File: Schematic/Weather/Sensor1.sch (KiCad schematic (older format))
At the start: 2 parts

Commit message: Start PCB
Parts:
- MOD1: footprint (none) -> footprint:HTU21
- MOD2: footprint (none) -> footprint:BMP180
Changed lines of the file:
@@
 F 0 "MOD2" H 5678 1771 50  0000 L CNN
 F 1 "BMP180" H 5678 1680 50  0000 L CNN
-F 2 "" H 5250 1350 50  0001 C CNN
+F 2 "footprint:BMP180" H 5250 1350 50  0001 C CNN
 F 3 "" H 5250 1350 50  0001 C CNN
 	1    5050 1850
@@
 F 0 "MOD1" H 5628 2846 50  0000 L CNN
 F 1 "HTU21" H 5628 2755 50  0000 L CNN
-F 2 "" H 5200 2550 50  0001 C CNN
+F 2 "footprint:HTU21" H 5200 2550 50  0001 C CNN
 F 3 "" H 5200 2550 50  0001 C CNN
 	1    5000 2850

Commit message: small compnent changes
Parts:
- MOD1: symbol MyComponents:HTU21 -> Weather-rescue:HTU21-MyComponents
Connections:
- wire segments 23 -> 24
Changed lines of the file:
@@
 J4_P4
+$Comp
+L Weather-rescue:HTU21-MyComponents MOD1
+U 1 1 5C959FE9
+P 5000 2850
+AR Path="/5C959FE9" Ref="MOD1"  Part="1"
+AR Path="/5C9254A0/5C959FE9" Ref="MOD1"  Part="1"
+F 0 "MOD1" H 5628 2846 50  0000 L CNN
+F 1 "HTU21" H 5628 2755 50  0000 L CNN
+F 2 "footprint:HTU21" H 5200 2550 50  0001 C CNN
+F 3 "" H 5200 2550 50  0001 C CNN
+	1    5000 2850
+	1    0    0    -1
+$EndComp
+Wire Wire Line
+	4000 1750 2650 1750
+Wire Wire Line
+	2650 2200 3700 2200
+Wire Wire Line
+	4900 3200 3700 3200
+Wire Wire Line
+	4650 2750 4900 2750
+Wire Wire Line
+	2650 2050 3000 2050
+Wire Wire Line
+	3000 2050 3000 2400
+Wire Wire Line
+	3000 2400 4550 2400
+Wire Wire Line
+	2650 1900 3300 1900
+Wire Wire Line
+	3300 1900 3300 2300
+Wire Wire Line
+	3300 2300 4650 2300
+Wire Wire Line
+	4650 2300 4650 2750
 $Comp
 L MyComponents:BMP180 MOD2
@@
 	1    0    0    -1
 $EndComp
-$Comp
-L MyComponents:HTU21 MOD1
-U 1 1 5C959FE9
-P 5000 2850
-F 0 "MOD1" H 5628 2846 50  0000 L CNN
-F 1 "HTU21" H 5628 2755 50  0000 L CNN
-F 2 "footprint:HTU21" H 5200 2550 50  0001 C CNN
-F 3 "" H 5200 2550 50  0001 C CNN
-	1    5000 2850
-	1    0    0    -1
-$EndComp
-Wire Wire Line
-	4950 1750 4000 1750
-Wire Wire Line
-	4900 2900 4000 2900
-Wire Wire Line
-	4000 2900 4000 1750
-Connection ~ 4000 1750
-Wire Wire Line
-	4000 1750 2650 1750
-Wire Wire Line
-	2650 2200 3700 2200
-Wire Wire Line
-	3700 2200 3700 1900
-Wire Wire Line
-	3700 1900 4950 1900
-Wire Wire Line
-	4900 3200 3700 3200
 Wire Wire Line
 	3700 3200 3700 2200
+Wire Wire Line
+	4950 2200 3700 2200
 Connection ~ 3700 2200
 Wire Wire Line
-	4950 2050 4650 2050
+	4000 2050 4000 1750
 Wire Wire Line
-	4650 2050 4650 2300
+	4950 2050 4000 2050
 Wire Wire Line
-	4650 2750 4900 2750
+	4950 1900 4800 1900
 Wire Wire Line
-	4950 2200 4800 2200
+	4800 1900 4800 2400
 Wire Wire Line
-	4800 2200 4800 2400
+	4950 1750 4650 1750
 Wire Wire Line
-	4800 2600 4900 2600
-Wire Wire Line
-	2650 2050 3000 2050
-Wire Wire Line
-	3000 2050 3000 2400
-Wire Wire Line
-	3000 2400 4800 2400
-Connection ~ 4800 2400
-Wire Wire Line
-	4800 2400 4800 2600
-Wire Wire Line
-	2650 1900 3300 1900
-Wire Wire Line
-	3300 1900 3300 2300
-Wire Wire Line
-	3300 2300 4650 2300
+	4650 1750 4650 2300
 Connection ~ 4650 2300
 Wire Wire Line
-	4650 2300 4650 2750
+	4900 2900 4550 2900
+Wire Wire Line
+	4550 2900 4550 2400
+Connection ~ 4550 2400
+Wire Wire Line
+	4550 2400 4800 2400
+Wire Wire Line
+	4900 3050 4000 3050
+Wire Wire Line
+	4000 3050 4000 2050
+Connection ~ 4000 2050
 $EndSCHEMATC

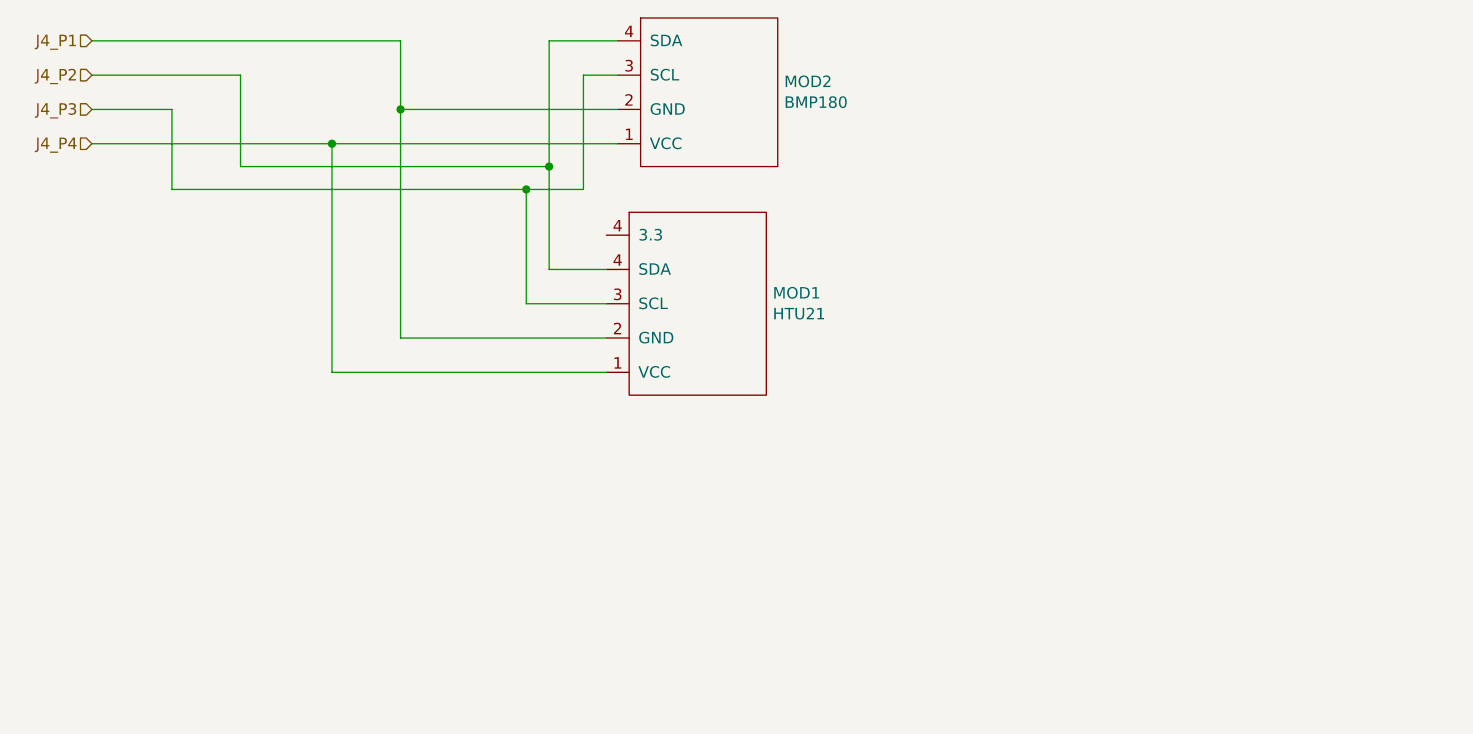
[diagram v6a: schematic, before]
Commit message: Board update 4 channels
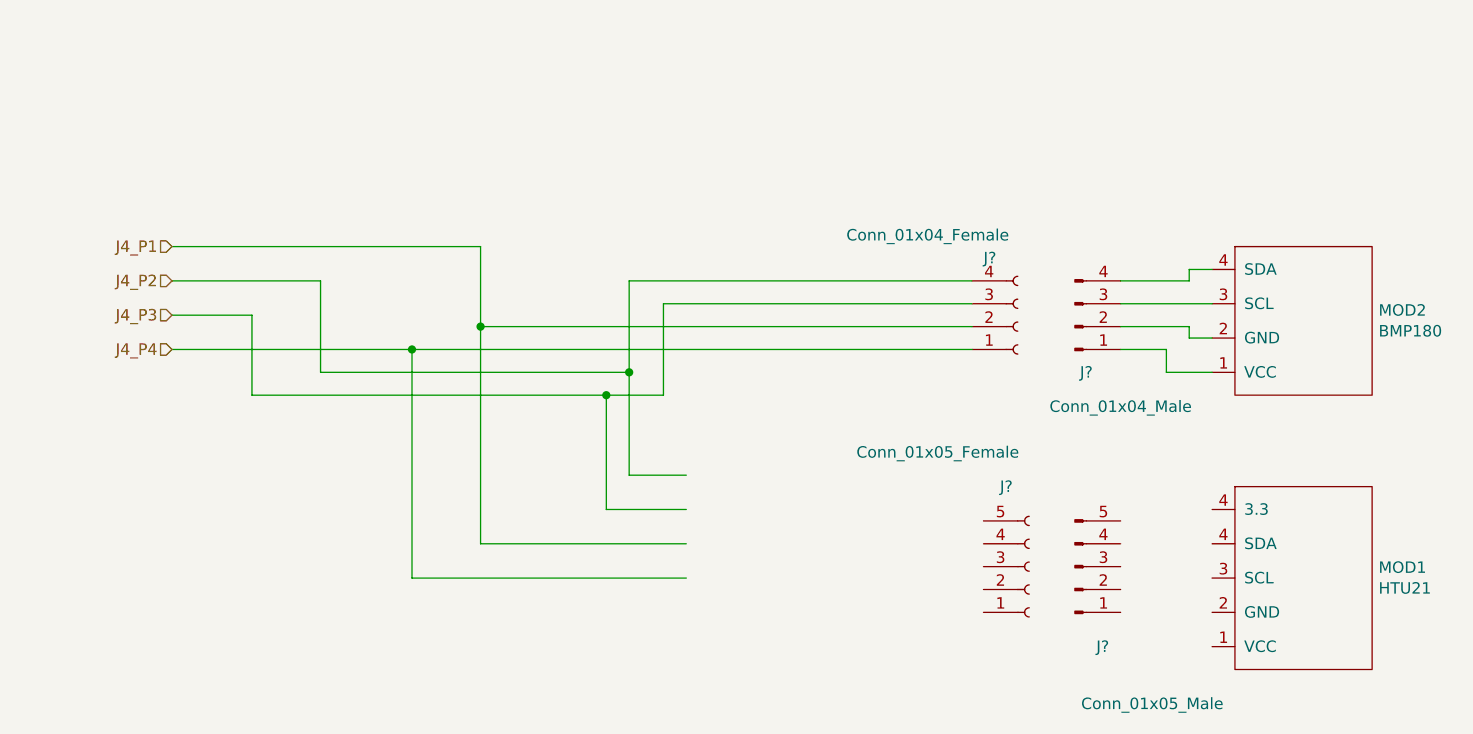
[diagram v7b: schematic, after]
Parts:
- added J?: Conn_01x04_Female, symbol Connector:Conn_01x04_Female
- added J?: Conn_01x04_Male, symbol Connector:Conn_01x04_Male
- added J?: Conn_01x05_Female, symbol Connector:Conn_01x05_Female
- added J?: Conn_01x05_Male, symbol Connector:Conn_01x05_Male
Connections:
- wire segments 24 -> 34
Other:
- moved on the sheet: MOD1, MOD2
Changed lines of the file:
@@
 Comment4 ""
 $EndDescr
-Text HLabel 2650 1750 0    50   Input ~ 0
+Text HLabel 3000 2650 0    50   Input ~ 0
 J4_P1
-Text HLabel 2650 1900 0    50   Input ~ 0
+Text HLabel 3000 2800 0    50   Input ~ 0
 J4_P2
-Text HLabel 2650 2050 0    50   Input ~ 0
+Text HLabel 3000 2950 0    50   Input ~ 0
 J4_P3
-Text HLabel 2650 2200 0    50   Input ~ 0
+Text HLabel 3000 3100 0    50   Input ~ 0
 J4_P4
+Wire Wire Line
+	4350 2650 3000 2650
+Wire Wire Line
+	3000 3100 4050 3100
+Wire Wire Line
+	3000 2950 3350 2950
+Wire Wire Line
+	3350 2950 3350 3300
+Wire Wire Line
+	3350 3300 4900 3300
+Wire Wire Line
+	3000 2800 3650 2800
+Wire Wire Line
+	3650 2800 3650 3200
+Wire Wire Line
+	3650 3200 5000 3200
+Wire Wire Line
+	5000 3200 5000 3650
+Wire Wire Line
+	4050 4100 4050 3100
+Connection ~ 4050 3100
+Wire Wire Line
+	4900 3800 4900 3300
+Connection ~ 4900 3300
+Wire Wire Line
+	4900 3300 5150 3300
+Wire Wire Line
+	4350 3950 4350 3000
+$Comp
+L Connector:Conn_01x04_Male J?
+U 1 1 5CAF11D2
+P 6950 3000
+F 0 "J?" H 7000 3200 50  0000 C CNN
+F 1 "Conn_01x04_Male" H 7150 3350 50  0000 C CNN
+F 2 "" H 6950 3000 50  0001 C CNN
+F 3 "~" H 6950 3000 50  0001 C CNN
+	1    6950 3000
+	1    0    0    1
+$EndComp
+$Comp
+L Connector:Conn_01x05_Male J?
+U 1 1 5CAF34CD
+P 6950 4050
+F 0 "J?" H 7100 4400 50  0000 R CNN
+F 1 "Conn_01x05_Male" H 7600 4650 50  0000 R CNN
+F 2 "" H 6950 4050 50  0001 C CNN
+F 3 "~" H 6950 4050 50  0001 C CNN
+	1    6950 4050
+	1    0    0    1
+$EndComp
+Wire Wire Line
+	5250 3950 4350 3950
+Wire Wire Line
+	5250 3800 4900 3800
+Wire Wire Line
+	5000 3650 5250 3650
+Wire Wire Line
+	5250 4100 4050 4100
 $Comp
 L Weather-rescue:HTU21-MyComponents MOD?
 U 1 1 5C959FE9
-P 5000 2850
+P 7650 4050
 AR Path="/5C959FE9" Ref="MOD?"  Part="1"
 AR Path="/5C9254A0/5C959FE9" Ref="MOD1"  Part="1"
-F 0 "MOD1" H 5628 2846 50  0000 L CNN
-F 1 "HTU21" H 5628 2755 50  0000 L CNN
-F 2 "footprint:HTU21" H 5200 2550 50  0001 C CNN
-F 3 "" H 5200 2550 50  0001 C CNN
-	1    5000 2850
+F 0 "MOD1" H 8278 4046 50  0000 L CNN
+F 1 "HTU21" H 8278 3955 50  0000 L CNN
+F 2 "footprint:HTU21" H 7850 3750 50  0001 C CNN
+F 3 "" H 7850 3750 50  0001 C CNN
+	1    7650 4050
 	1    0    0    -1
 $EndComp
-Wire Wire Line
-	4000 1750 2650 1750
-Wire Wire Line
-	2650 2200 3700 2200
-Wire Wire Line
-	4900 3200 3700 3200
-Wire Wire Line
-	4650 2750 4900 2750
-Wire Wire Line
-	2650 2050 3000 2050
-Wire Wire Line
-	3000 2050 3000 2400
-Wire Wire Line
-	3000 2400 4550 2400
-Wire Wire Line
-	2650 1900 3300 1900
-Wire Wire Line
-	3300 1900 3300 2300
-Wire Wire Line
-	3300 2300 4650 2300
-Wire Wire Line
-	4650 2300 4650 2750
 $Comp
 L MyComponents:BMP180 MOD2
 U 1 1 5C958DD2
-P 5050 1850
-F 0 "MOD2" H 5678 1771 50  0000 L CNN
-F 1 "BMP180" H 5678 1680 50  0000 L CNN
-F 2 "footprint:BMP180" H 5250 1350 50  0001 C CNN
-F 3 "" H 5250 1350 50  0001 C CNN
-	1    5050 1850
+P 7650 2850
+F 0 "MOD2" H 8278 2771 50  0000 L CNN
+F 1 "BMP180" H 8278 2680 50  0000 L CNN
+F 2 "footprint:BMP180" H 7850 2350 50  0001 C CNN
+F 3 "" H 7850 2350 50  0001 C CNN
+	1    7650 2850
 	1    0    0    -1
 $EndComp
+$Comp
+L Connector:Conn_01x04_Female J?
+U 1 1 5CAF0516
+P 6700 3000
+F 0 "J?" H 6550 2700 50  0000 L CNN
+F 1 "Conn_01x04_Female" H 5950 2600 50  0000 L CNN
+F 2 "" H 6700 3000 50  0001 C CNN
+F 3 "~" H 6700 3000 50  0001 C CNN
+	1    6700 3000
+	1    0    0    1
+$EndComp
+Connection ~ 5000 3200
 Wire Wire Line
-	3700 3200 3700 2200
+	4050 3100 6500 3100
 Wire Wire Line
-	4950 2200 3700 2200
-Connection ~ 3700 2200
+	7150 3100 7350 3100
 Wire Wire Line
-	4000 2050 4000 1750
+	7350 3100 7350 3200
 Wire Wire Line
-	4950 2050 4000 2050
+	7350 3200 7550 3200
 Wire Wire Line
-	4950 1900 4800 1900
+	7150 3000 7450 3000
 Wire Wire Line
-	4800 1900 4800 2400
+	7450 3000 7450 3050
 Wire Wire Line
-	4950 1750 4650 1750
+	7450 3050 7550 3050
 Wire Wire Line
-	4650 1750 4650 2300
-Connection ~ 4650 2300
+	7150 2900 7550 2900
 Wire Wire Line
-	4900 2900 4550 2900
+	7150 2800 7450 2800
 Wire Wire Line
-	4550 2900 4550 2400
-Connection ~ 4550 2400
+	7450 2800 7450 2750
 Wire Wire Line
-	4550 2400 4800 2400
+	7450 2750 7550 2750
 Wire Wire Line
-	4900 3050 4000 3050
+	6500 3000 4350 3000
+Connection ~ 4350 3000
 Wire Wire Line
-	4000 3050 4000 2050
-Connection ~ 4000 2050
+	5000 2800 5000 3200
+Wire Wire Line
+	5150 2900 5150 3300
+Wire Wire Line
+	6500 2900 5150 2900
+Wire Wire Line
+	4350 2650 4350 3000
+Wire Wire Line
+	5000 2800 6500 2800
+$Comp
+L Connector:Conn_01x05_Female J?
+U 1 1 5CAF2250
+P 6750 4050
+F 0 "J?" H 6650 3700 50  0000 C CNN
+F 1 "Conn_01x05_Female" H 6350 3550 50  0000 C CNN
+F 2 "" H 6750 4050 50  0001 C CNN
+F 3 "~" H 6750 4050 50  0001 C CNN
+	1    6750 4050
+	1    0    0    1
+$EndComp
 $EndSCHEMATC

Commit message: new M_Board internal
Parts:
- J11, J13: renamed from J?; footprint (none) -> Connector_PinHeader_2.54mm:PinHeader_1x04_P2.54mm_Vertical
- J12, J14: renamed from J?; footprint (none) -> Connector_PinHeader_2.54mm:PinHeader_1x05_P2.54mm_Vertical
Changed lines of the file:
@@
 $Descr A4 11693 8268
 encoding utf-8
-Sheet 4 13
+Sheet 4 14
 Title ""
 Date ""
@@
 	4350 3950 4350 3000
 $Comp
-L Connector:Conn_01x04_Male J?
+L Connector:Conn_01x04_Male J13
 U 1 1 5CAF11D2
 P 6950 3000
-F 0 "J?" H 7000 3200 50  0000 C CNN
+F 0 "J13" H 7000 3200 50  0000 C CNN
 F 1 "Conn_01x04_Male" H 7150 3350 50  0000 C CNN
-F 2 "" H 6950 3000 50  0001 C CNN
+F 2 "Connector_PinHeader_2.54mm:PinHeader_1x04_P2.54mm_Vertical" H 6950 3000 50  0001 C CNN
 F 3 "~" H 6950 3000 50  0001 C CNN
 	1    6950 3000
@@
 $EndComp
 $Comp
-L Connector:Conn_01x05_Male J?
+L Connector:Conn_01x05_Male J14
 U 1 1 5CAF34CD
 P 6950 4050
-F 0 "J?" H 7100 4400 50  0000 R CNN
+F 0 "J14" H 7100 4400 50  0000 R CNN
 F 1 "Conn_01x05_Male" H 7600 4650 50  0000 R CNN
-F 2 "" H 6950 4050 50  0001 C CNN
+F 2 "Connector_PinHeader_2.54mm:PinHeader_1x05_P2.54mm_Vertical" H 6950 4050 50  0001 C CNN
 F 3 "~" H 6950 4050 50  0001 C CNN
 	1    6950 4050
@@
 $EndComp
 $Comp
-L Connector:Conn_01x04_Female J?
+L Connector:Conn_01x04_Female J11
 U 1 1 5CAF0516
 P 6700 3000
-F 0 "J?" H 6550 2700 50  0000 L CNN
+F 0 "J11" H 6550 2700 50  0000 L CNN
 F 1 "Conn_01x04_Female" H 5950 2600 50  0000 L CNN
-F 2 "" H 6700 3000 50  0001 C CNN
+F 2 "Connector_PinHeader_2.54mm:PinHeader_1x04_P2.54mm_Vertical" H 6700 3000 50  0001 C CNN
 F 3 "~" H 6700 3000 50  0001 C CNN
 	1    6700 3000
@@
 	5000 2800 6500 2800
 $Comp
-L Connector:Conn_01x05_Female J?
+L Connector:Conn_01x05_Female J12
 U 1 1 5CAF2250
 P 6750 4050
-F 0 "J?" H 6650 3700 50  0000 C CNN
+F 0 "J12" H 6650 3700 50  0000 C CNN
 F 1 "Conn_01x05_Female" H 6350 3550 50  0000 C CNN
-F 2 "" H 6750 4050 50  0001 C CNN
+F 2 "Connector_PinHeader_2.54mm:PinHeader_1x05_P2.54mm_Vertical" H 6750 4050 50  0001 C CNN
 F 3 "~" H 6750 4050 50  0001 C CNN
 	1    6750 4050
